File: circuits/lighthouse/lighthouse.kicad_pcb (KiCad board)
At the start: 2 copper layers, 4 parts, among them U1 ESP32 CP2102, U3 DCDC_StepUp_SX1308

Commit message: Circuits
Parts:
- added D1: LED, LED_SMD:LED_1206_3216Metric_Pad1.42x1.75mm_HandSolder, F.Cu at (117.8, 91.8)
- added D2: LED, LED_SMD:LED_1206_3216Metric_Pad1.42x1.75mm_HandSolder, F.Cu at (117.8, 94.8)
- added D3: LED, LED_SMD:LED_1206_3216Metric_Pad1.42x1.75mm_HandSolder, F.Cu at (117.8, 97.8)
- added D4: LED, LED_SMD:LED_1206_3216Metric_Pad1.42x1.75mm_HandSolder, F.Cu at (117.8, 100.8)
- added Q1: S9013, Package_TO_SOT_THT:TO-92_Inline, F.Cu at (125.3, 86.8)
- added R1: 10k, Resistor_SMD:R_1206_3216Metric_Pad1.30x1.75mm_HandSolder, F.Cu at (117.8, 103.8)
- added R2: 20k, Resistor_SMD:R_1206_3216Metric_Pad1.30x1.75mm_HandSolder, F.Cu at (123.8, 103.8)
- added R3: 1k, Resistor_SMD:R_1206_3216Metric_Pad1.30x1.75mm_HandSolder, F.Cu at (123.8, 91.8)
- added R4: 1k, Resistor_SMD:R_1206_3216Metric_Pad1.30x1.75mm_HandSolder, F.Cu at (123.8, 94.8)
- added R5: 1k, Resistor_SMD:R_1206_3216Metric_Pad1.30x1.75mm_HandSolder, F.Cu at (123.8, 97.8)
- added R6: 1k, Resistor_SMD:R_1206_3216Metric_Pad1.30x1.75mm_HandSolder, F.Cu at (123.8, 100.8)
- added R7: 240, LED_SMD:LED_1206_3216Metric_Pad1.42x1.75mm_HandSolder, F.Cu at (117.8, 88.8)
- added U2: DCDC_StepUp_SX1308, SX1308_DCDC_boost:DCDC_StepUp_SX1308, F.Cu at (91.0, 113.1)
- BT1: footprint Battery:BatteryHolder_MPD_BK-18650-PC2 -> Battery:BatteryHolder_MPD_BH-18650-PC
- U3: value DCDC_StepUp_SX1308 -> ~; footprint SX1308_DCDC_boost:DCDC_StepUp_SX1308 -> YR300:YR300
- moved U1 79.6 mm to (109.8, 94.8), turned to -90 degrees
- moved BT1 68.9 mm to (61.2, 140.3)
- moved CH1 68.6 mm to (72.8, 118.7)
- moved U3 67.2 mm to (119.3, 80.8), turned to 90 degrees
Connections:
- U1 pad 16: unconnected-(U1-GPIO9_/_SO2-Pad16) -> RX
- U1 pad 17: unconnected-(U1-GPIO10__/_S03-Pad17) -> TX
- U1 pad 19: Net-(U1-V5) -> 5V
- U1 pad 3: unconnected-(U1-GPIO36-Pad3) -> RFID_PW
- U1 pad 36: unconnected-(U1-GPIO22-Pad36) -> PWR_SENSE
- U1 pad 38: Net-(U1-GND-Pad38) -> GND
- U1 pad 4: unconnected-(U1-GPIO39-Pad4) -> MQTT_STS
- U1 pad 5: unconnected-(U1-GPIO34-Pad5) -> WIFI_STS
- U1 pad 6: unconnected-(U1-GPIO35-Pad6) -> SCAN_DETECTED
- U1 pad 7: unconnected-(U1-GPIO32-Pad7) -> ACTIVE_SCAN
- U3 pad 1: Net-(CH1-+OUT) -> 5V
- U3 pad 2: Net-(CH1--OUT) -> TX
- U3 pad 3: Net-(U1-GND-Pad38) -> RX
- U3 pad 4: Net-(U1-V5) -> Net-(Q1-C)
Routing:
- net 5V: track 0.00 -> 135.6 mm
- net Net-(U1-GND-Pad38): track 73.9 -> 0.00 mm
- net GND: track 0.00 -> 67.4 mm
- net Net-(Q1-C): track 0.00 -> 51.7 mm
- net ACTIVE_SCAN: track 0.00 -> 29.6 mm
- net SCAN_DETECTED: track 0.00 -> 25.8 mm
- net WIFI_STS: track 0.00 -> 22.1 mm
- net PWR_SENSE: track 0.00 -> 20.5 mm
- net Net-(BT1--): track 61.5 -> 80.3 mm
- net MQTT_STS: track 0.00 -> 18.3 mm
- net RFID_PW: track 0.00 -> 14.6 mm
- net Net-(U1-V5): track 12.2 -> 0.00 mm
- net Net-(Q1-B): track 0.00 -> 5.85 mm
- net RX: track 0.00 -> 5.21 mm
- net TX: track 0.00 -> 4.71 mm
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
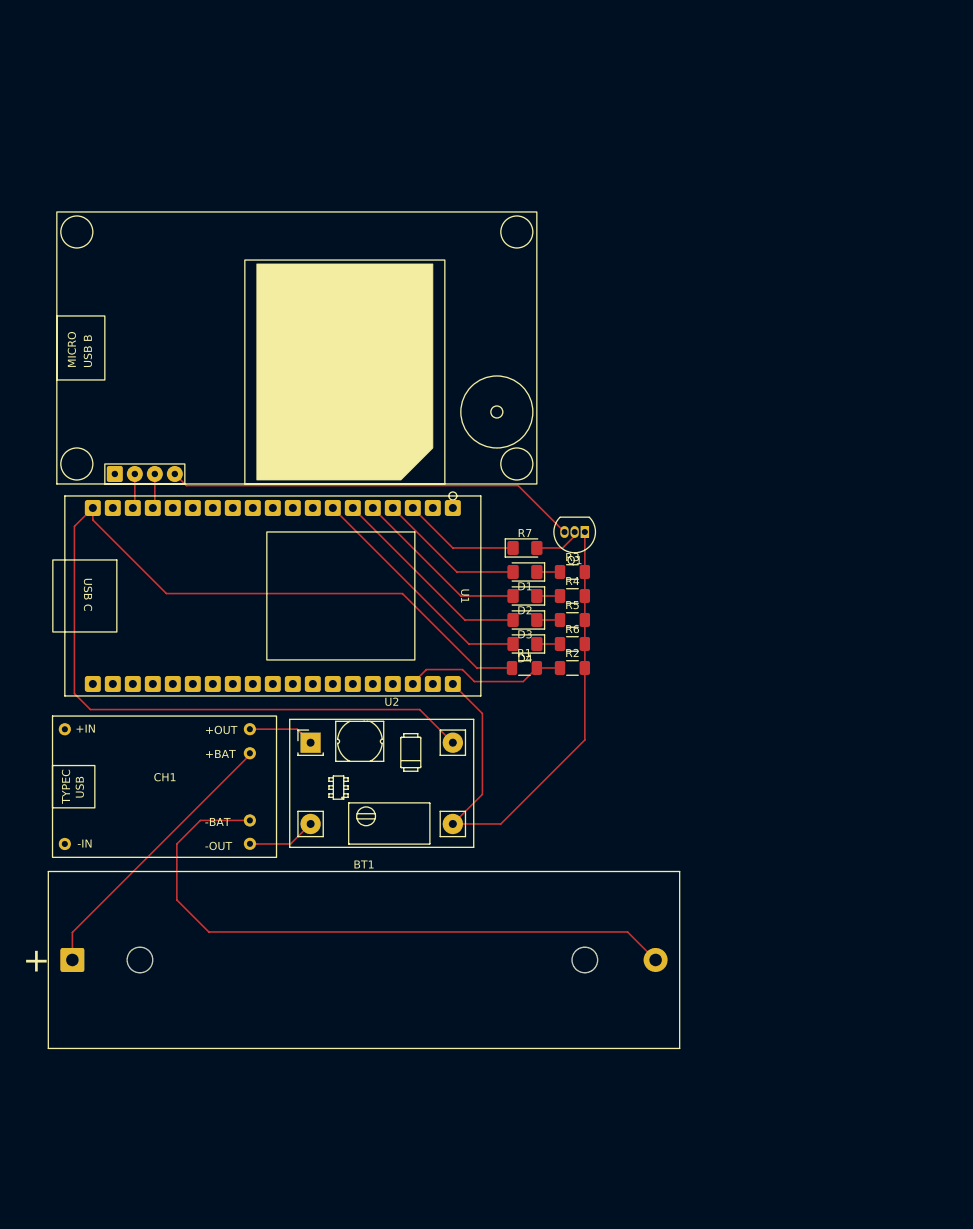
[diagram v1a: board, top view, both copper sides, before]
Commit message: Reverse engineered cell charger (component values missing)
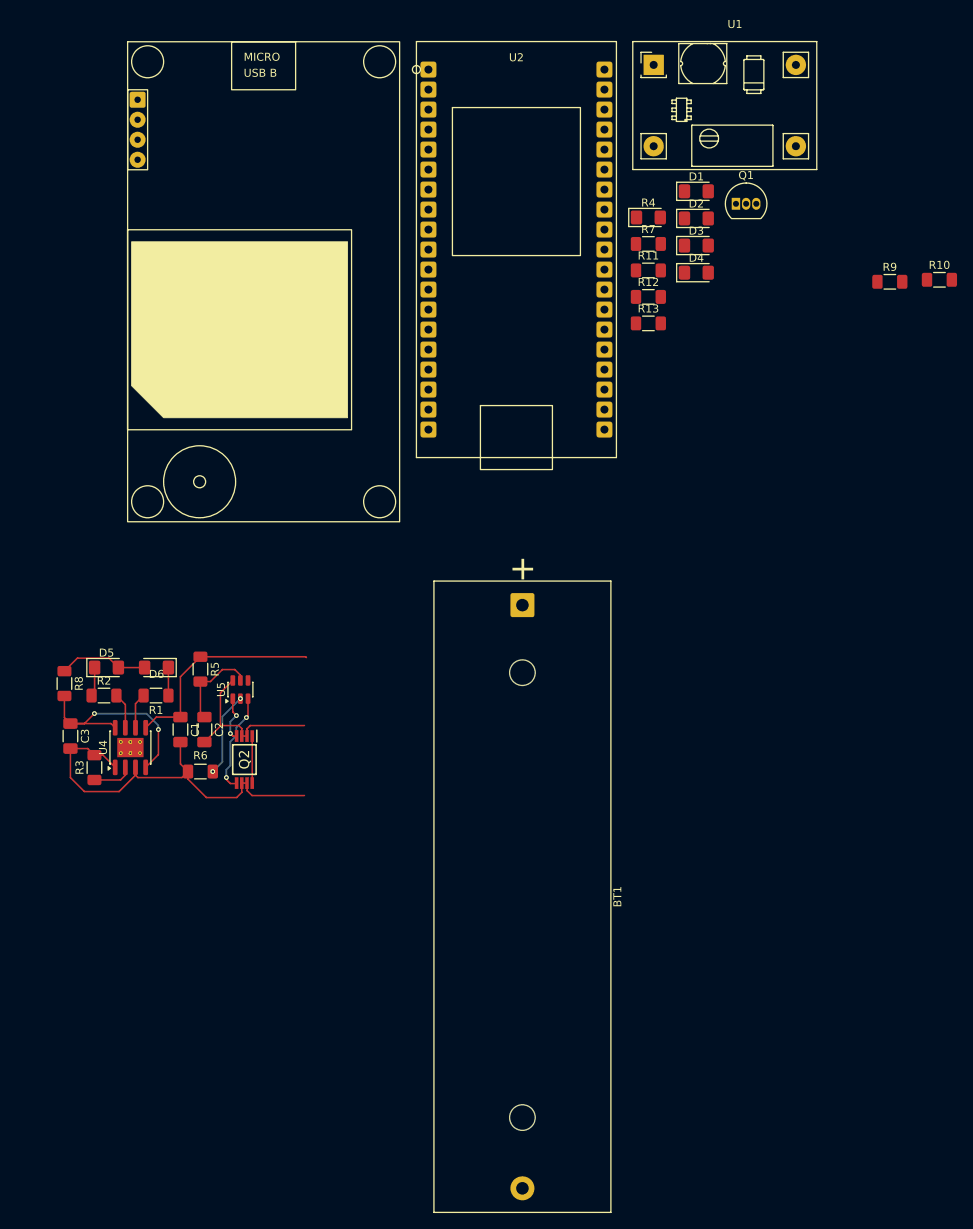
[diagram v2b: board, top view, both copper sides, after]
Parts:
- removed CH1: ~, TP4056_Charging_module:TP4056_Charging_Module_Type_C
- added C1: C, Capacitor_SMD:C_1206_3216Metric_Pad1.33x1.80mm_HandSolder, F.Cu at (74.8, 111.5)
- added C2: C, Capacitor_SMD:C_1206_3216Metric_Pad1.33x1.80mm_HandSolder, F.Cu at (77.8, 111.5)
- added C3: C, Capacitor_SMD:C_1206_3216Metric_Pad1.33x1.80mm_HandSolder, F.Cu at (61.0, 112.3)
- added D5: D, LED_SMD:LED_1206_3216Metric_Pad1.42x1.75mm_HandSolder, F.Cu at (65.5, 103.8)
- added D6: D, LED_SMD:LED_1206_3216Metric_Pad1.42x1.75mm_HandSolder, F.Cu at (71.8, 103.8)
- added Q2: FS8205A, FS8205A:SOP65P640X120-8N, F.Cu at (82.8, 115.2)
- added R10: 1k, Resistor_SMD:R_1206_3216Metric_Pad1.30x1.75mm_HandSolder, F.Cu at (169.6, 55.3)
- added R11: 1k, Resistor_SMD:R_1206_3216Metric_Pad1.30x1.75mm_HandSolder, F.Cu at (133.2, 54.1)
- added R12: 1k, Resistor_SMD:R_1206_3216Metric_Pad1.30x1.75mm_HandSolder, F.Cu at (133.2, 57.4)
- added R13: 1k, Resistor_SMD:R_1206_3216Metric_Pad1.30x1.75mm_HandSolder, F.Cu at (133.2, 60.7)
- added R8: R, Resistor_SMD:R_1206_3216Metric_Pad1.30x1.75mm_HandSolder, F.Cu at (60.2, 105.8)
- added R9: 20k, Resistor_SMD:R_1206_3216Metric_Pad1.30x1.75mm_HandSolder, F.Cu at (163.4, 55.5)
- added U4: TP4056-42-ESOP8, Package_SO:SOIC-8-1EP_3.9x4.9mm_P1.27mm_EP2.41x3.3mm_ThermalVias, F.Cu at (68.5, 113.8)
- added U5: DW01A, Package_TO_SOT_SMD:SOT-23-6, F.Cu at (82.2, 106.5)
- R1: value 10k -> 1k
- R2: value 20k -> 1k
- R3, R5, R6: value 1k -> R
- R4: value 1k -> 240; footprint Resistor_SMD:R_1206_3216Metric_Pad1.30x1.75mm_HandSolder -> LED_SMD:LED_1206_3216Metric_Pad1.42x1.75mm_HandSolder
- R7: value 240 -> 10k; footprint LED_SMD:LED_1206_3216Metric_Pad1.42x1.75mm_HandSolder -> Resistor_SMD:R_1206_3216Metric_Pad1.30x1.75mm_HandSolder
- U1: value ESP32 CP2102 -> DCDC_StepUp_SX1308; footprint ESP32:ESP32_38Pin -> SX1308_DCDC_boost:DCDC_StepUp_SX1308
- U2: value DCDC_StepUp_SX1308 -> ESP32 CP2102; footprint SX1308_DCDC_boost:DCDC_StepUp_SX1308 -> ESP32:ESP32_38Pin
- moved U2 88.9 mm to (116.8, 28.0)
- moved BT1 71.6 mm to (117.5, 95.9), turned to -90 degrees
- moved U1 70.6 mm to (133.9, 28.4), turned to 0 degrees
- moved R3 64.6 mm to (64.0, 116.2), turned to 90 degrees
- moved R2 58.7 mm to (65.2, 107.2)
- moved D1 52.2 mm to (139.2, 44.2), turned to 0 degrees
- moved D2 51.8 mm to (139.2, 47.6), turned to 0 degrees
- moved D3 51.5 mm to (139.2, 51.0), turned to 0 degrees
- moved U3 51.4 mm to (68.2, 85.5), turned to 0 degrees
- moved D4 51.1 mm to (139.2, 54.4), turned to 0 degrees
- moved R6 49.2 mm to (77.2, 116.8)
- moved R4 48.3 mm to (133.2, 47.5)
- moved R5 46.9 mm to (77.2, 104.0), turned to -90 degrees
- moved R1 46.2 mm to (71.7, 107.2), turned to 180 degrees
- moved Q1 45.2 mm to (144.2, 45.8), turned to 0 degrees
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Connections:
- BT1 pad 1: Net-(BT1-+) -> /Charger/+BAT
- BT1 pad 2: Net-(BT1--) -> /Charger/-BAT
- R1 pad 1: 5V -> Net-(D6-K)
- R1 pad 2: PWR_SENSE -> Net-(U4-~{STDBY})
- R2 pad 1: PWR_SENSE -> Net-(D5-K)
- R2 pad 2: GND -> Net-(U4-~{CHRG})
- R3 pad 1: Net-(D1-K) -> Net-(U4-PROG)
- R3 pad 2: GND -> /Charger/-IN
- R4 pad 1: Net-(D2-K) -> RFID_PW
- R4 pad 2: GND -> Net-(Q1-B)
- R5 pad 1: Net-(D3-K) -> /Charger/+BAT
- R5 pad 2: GND -> Net-(U5-VCC)
- R6 pad 1: Net-(D4-K) -> /Charger/-IN
- R6 pad 2: GND -> Net-(U5-CS)
- R7 pad 1: RFID_PW -> 5V
- R7 pad 2: Net-(Q1-B) -> PWR_SENSE
- U1 pad 1: unconnected-(U1-3V3-Pad1) -> /Charger/+BAT
- U1 pad 2: unconnected-(U1-EN-Pad2) -> /Charger/-IN
- U1 pad 3: RFID_PW -> GND
- U1 pad 4: MQTT_STS -> 5V
- U2 pad 1: Net-(CH1-+OUT) -> unconnected-(U2-3V3-Pad1)
- U2 pad 2: Net-(CH1--OUT) -> unconnected-(U2-EN-Pad2)
- U2 pad 3: GND -> RFID_PW
- U2 pad 4: 5V -> MQTT_STS
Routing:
- net 5V: track 135.6 -> 0.00 mm
- net Net-(BT1--): track 80.3 -> 0.00 mm
- net GND: track 67.4 -> 0.00 mm
- net Net-(Q1-C): track 51.7 -> 0.00 mm
- net /Charger/-IN: track 0.00 -> 51.0 mm
- net Net-(BT1-+): track 35.0 -> 0.00 mm
- net ACTIVE_SCAN: track 29.6 -> 0.00 mm
- net /Charger/+IN: track 0.00 -> 28.3 mm, vias 0 -> 2
- net /Charger/+BAT: track 0.00 -> 26.8 mm
- net SCAN_DETECTED: track 25.8 -> 0.00 mm
- net WIFI_STS: track 22.1 -> 0.00 mm
- net /Charger/-BAT: track 0.00 -> 21.8 mm
- net PWR_SENSE: track 20.5 -> 0.00 mm
- net MQTT_STS: track 18.3 -> 0.00 mm
- net RFID_PW: track 14.6 -> 0.00 mm
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
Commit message: More circuits
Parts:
- removed U3: ~, YR300:YR300
- added AE1: Antenna_Shield, Connector_Coaxial:SMA_Samtec_SMA-J-P-H-ST-EM1_EdgeMount, F.Cu at (95.9, 63.4)
- added BOOT1: SW_Push, Button_Switch_SMD:SW_Push_SPST_NO_Alps_SKRK, F.Cu at (-42.9, 104.0)
- added BZ1: Buzzer, Buzzer_Beeper:Buzzer_12x9.5RM7.6, F.Cu at (176.4, 60.7)
- added C10: C, Capacitor_SMD:C_1206_3216Metric_Pad1.33x1.80mm_HandSolder, F.Cu at (-33.7, 33.0)
- added C11: C, Capacitor_SMD:C_1206_3216Metric_Pad1.33x1.80mm_HandSolder, F.Cu at (-94.4, 94.8)
- added C12: C, Capacitor_SMD:C_1206_3216Metric_Pad1.33x1.80mm_HandSolder, F.Cu at (-94.4, 98.2)
- added C13: C, Capacitor_SMD:C_1206_3216Metric_Pad1.33x1.80mm_HandSolder, F.Cu at (-94.4, 101.5)
- added C4: C, Capacitor_SMD:C_1206_3216Metric_Pad1.33x1.80mm_HandSolder, F.Cu at (83.1, 127.2)
- added C5: C, Capacitor_SMD:C_1206_3216Metric_Pad1.33x1.80mm_HandSolder, F.Cu at (98.6, 122.8)
- added C6: C, Capacitor_SMD:C_1206_3216Metric_Pad1.33x1.80mm_HandSolder, F.Cu at (137.1, 122.5)
- added C7: C, Capacitor_SMD:C_1206_3216Metric_Pad1.33x1.80mm_HandSolder, F.Cu at (137.1, 120.0)
- added C8: C, Capacitor_SMD:C_1206_3216Metric_Pad1.33x1.80mm_HandSolder, F.Cu at (138.6, 92.7)
- added C9: C, Capacitor_SMD:C_1206_3216Metric_Pad1.33x1.80mm_HandSolder, F.Cu at (138.6, 96.0)
- added D10: D, LED_SMD:LED_1206_3216Metric_Pad1.42x1.75mm_HandSolder, F.Cu at (168.6, 64.3)
- added D11: LED, LED_SMD:LED_1206_3216Metric_Pad1.42x1.75mm_HandSolder, F.Cu at (133.1, 121.2)
- added D12: D_Schottky, Diode_SMD:D_2114_3652Metric_Pad1.85x3.75mm_HandSolder, F.Cu at (-63.1, 94.8)
- added D13: LED, LED_SMD:LED_1206_3216Metric_Pad1.42x1.75mm_HandSolder, F.Cu at (-75.2, 112.1)
- added D14: LED, LED_SMD:LED_1206_3216Metric_Pad1.42x1.75mm_HandSolder, F.Cu at (-99.9, 70.0)
- added D7: D_Schottky, Diode_SMD:D_2114_3652Metric_Pad1.85x3.75mm_HandSolder, F.Cu at (94.4, 117.8)
- added D8: LED, LED_SMD:LED_1206_3216Metric_Pad1.42x1.75mm_HandSolder, F.Cu at (144.6, 86.0)
- added D9: LED, LED_SMD:LED_1206_3216Metric_Pad1.42x1.75mm_HandSolder, F.Cu at (144.6, 89.4)
- added EN1: SW_Push, Button_Switch_SMD:SW_Push_SPST_NO_Alps_SKRK, F.Cu at (-42.9, 108.5)
- added IC1: SX1308, SX1308:SOT95P280X145-6N, F.Cu at (91.6, 122.8)
- added L1: L, Inductor_THT:L_Radial_L8.0mm_W8.0mm_P5.00mm_Neosid_SD8, F.Cu at (84.6, 117.2)
- added Q3: 2N7002K, Package_TO_SOT_SMD:SOT-23, F.Cu at (166.5, 67.5)
- added Q4: SS8050, Package_TO_SOT_SMD:SOT-23, F.Cu at (-16.9, 11.0)
- added Q5: SS8050, Package_TO_SOT_SMD:SOT-23, F.Cu at (-16.9, 15.4)
- added R14: R, Resistor_SMD:R_1206_3216Metric_Pad1.30x1.75mm_HandSolder, F.Cu at (85.6, 127.2)
- added R15: R, Resistor_SMD:R_1206_3216Metric_Pad1.30x1.75mm_HandSolder, F.Cu at (109.1, 97.0)
- added R16: R, Resistor_SMD:R_1206_3216Metric_Pad1.30x1.75mm_HandSolder, F.Cu at (144.5, 100.7)
- added R17: R, Resistor_SMD:R_1206_3216Metric_Pad1.30x1.75mm_HandSolder, F.Cu at (159.7, 67.5)
- added R18: R, Resistor_SMD:R_1206_3216Metric_Pad1.30x1.75mm_HandSolder, F.Cu at (162.2, 67.5)
- added R19: R, Resistor_SMD:R_1206_3216Metric_Pad1.30x1.75mm_HandSolder, F.Cu at (140.9, 121.2)
- added R20: 10k, Resistor_SMD:R_1206_3216Metric_Pad1.30x1.75mm_HandSolder, F.Cu at (-44.4, 21.8)
- added R21: 10k, Resistor_SMD:R_1206_3216Metric_Pad1.30x1.75mm_HandSolder, F.Cu at (-112.2, 59.0)
- added R22: 10k, Resistor_SMD:R_1206_3216Metric_Pad1.30x1.75mm_HandSolder, F.Cu at (-112.2, 62.2)
- added R23: 1k, Resistor_SMD:R_1206_3216Metric_Pad1.30x1.75mm_HandSolder, F.Cu at (-112.2, 65.5)
- added R24: 1k, Resistor_SMD:R_1206_3216Metric_Pad1.30x1.75mm_HandSolder, F.Cu at (-75.7, 115.2)
- added R25: 10k, Resistor_SMD:R_1206_3216Metric_Pad1.30x1.75mm_HandSolder, F.Cu at (-75.7, 118.6)
- added R26: 10k, Resistor_SMD:R_1206_3216Metric_Pad1.30x1.75mm_HandSolder, F.Cu at (-40.3, 30.5)
- added R27: 10k, Resistor_SMD:R_1206_3216Metric_Pad1.30x1.75mm_HandSolder, F.Cu at (-27.6, 17.2)
- added R28: 1k, Resistor_SMD:R_1206_3216Metric_Pad1.30x1.75mm_HandSolder, F.Cu at (-29.4, 27.8)
- added R29: 1k, Resistor_SMD:R_1206_3216Metric_Pad1.30x1.75mm_HandSolder, F.Cu at (-21.2, 23.0)
- added R30: 10k, Resistor_SMD:R_1206_3216Metric_Pad1.30x1.75mm_HandSolder, F.Cu at (-37.9, 16.5)
- added R31: 1k, Resistor_SMD:R_1206_3216Metric_Pad1.30x1.75mm_HandSolder, F.Cu at (95.6, 122.8)
- added RV1: 8k4, Varistor:RV_Disc_D7mm_W4.9mm_P5mm, F.Cu at (95.1, 129.2)
- added U10: CP2102-GMR, CP2102-GMR:QFN28_5X5_SIL, F.Cu at (-35.9, 24.7)
- added U6: AMS1117-3.3, Package_TO_SOT_SMD:SOT-223-3_TabPin2, F.Cu at (162.9, 61.0)
- added U7: ESP32-WROOM-32, RF_Module:ESP32-WROOM-32, F.Cu at (61.3, 79.2)
- U1: value DCDC_StepUp_SX1308 -> R300; footprint SX1308_DCDC_boost:DCDC_StepUp_SX1308 -> YR300:R300
- U2: value ESP32 CP2102 -> AMS1117-3.3; footprint ESP32:ESP32_38Pin -> Package_TO_SOT_SMD:SOT-223-3_TabPin2
- moved R10 263.6 mm to (-93.9, 59.6)
- moved R9 257.3 mm to (-93.9, 56.3)
- moved D1 239.3 mm to (-99.9, 53.0)
- moved D2 239.3 mm to (-99.9, 56.4)
- moved D3 239.3 mm to (-99.9, 59.8)
- moved D4 239.3 mm to (-99.9, 63.2)
- moved R11 227.3 mm to (-93.9, 62.9)
- moved R12 227.3 mm to (-93.9, 66.2)
- moved R13 227.3 mm to (-93.9, 69.6)
- moved R7 227.2 mm to (-93.9, 53.0)
- moved U2 95.3 mm to (106.2, 122.7), turned to 180 degrees
- moved BT1 77.7 mm to (56.7, 144.2), turned to 0 degrees
- moved Q1 77.3 mm to (80.6, 89.8)
- moved R4 62.9 mm to (82.6, 84.8)
- moved U1 43.1 mm to (118.0, 68.5), turned to 180 degrees
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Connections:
- C1 pad 2: /Charger/-IN -> GND
- C3 pad 2: /Charger/-IN -> GND
- Q1 pad 3: Net-(Q1-C) -> /R300/GND
- Q2 pad 6: /Charger/-IN -> GND
- Q2 pad 7: /Charger/-IN -> GND
- R3 pad 2: /Charger/-IN -> GND
- R6 pad 1: /Charger/-IN -> GND
- R7 pad 2: PWR_SENSE -> Net-(U7-IO22)
- R9 pad 1: PWR_SENSE -> Net-(U7-IO22)
- U1 pad 1: /Charger/+BAT -> Net-(AE1-A)
- U1 pad 2: /Charger/-IN -> Net-(AE1-Shield)
- U1 pad 3: GND -> Net-(AE1-Shield)
- U1 pad 4: 5V -> Net-(AE1-Shield)
- U2 pad 1: unconnected-(U2-3V3-Pad1) -> GND
- U2 pad 2: unconnected-(U2-EN-Pad2) -> 3.3V
- U2 pad 3: RFID_PW -> 5V
- U4 pad 1: /Charger/-IN -> GND
- U4 pad 3: /Charger/-IN -> GND
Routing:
- net GND: track 0.00 -> 65.8 mm
- net /Charger/-BAT: track 21.8 -> 81.1 mm, vias 0 -> 1
- net /Charger/-IN: track 51.0 -> 0.00 mm
- net /Charger/+BAT: track 26.8 -> 73.3 mm, vias 0 -> 1
- net 5V: track 0.00 -> 27.7 mm
- net Net-(D7-A): track 0.00 -> 16.0 mm
- net Net-(BZ1--): track 0.00 -> 14.7 mm
- net Net-(AE1-Shield): track 0.00 -> 12.7 mm
- net Net-(D11-K): track 0.00 -> 8.52 mm
- net Net-(IC1-FB): track 0.00 -> 8.33 mm
- net Net-(Q3-G): track 0.00 -> 6.13 mm
- net Net-(C6-Pad1): track 0.00 -> 6.11 mm
- net /R300/GND: track 0.00 -> 6.09 mm
- net Net-(R14-Pad1): track 0.00 -> 5.14 mm
- net Net-(AE1-A): track 0.00 -> 4.97 mm

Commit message: The circuit now has all the values in place
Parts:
- added C14: 10u, Capacitor_SMD:C_1206_3216Metric_Pad1.33x1.80mm_HandSolder, F.Cu at (100.7, 105.4)
- added J1: USB_C_Receptacle_PowerOnly_6P, Connector_USB:USB_C_Receptacle_GCT_USB4125-xx-x_6P_TopMnt_Horizontal, F.Cu at (42.0, 111.4)
- added J2: USB_B_Micro, Connector_USB:USB_Micro-B_Amphenol_10103594-0001LF_Horizontal, F.Cu at (44.2, 96.5)
- added R32: 5k1, Resistor_SMD:R_1206_3216Metric_Pad1.30x1.75mm_HandSolder, F.Cu at (48.0, 114.1)
- added R33: 5k1, Resistor_SMD:R_1206_3216Metric_Pad1.30x1.75mm_HandSolder, F.Cu at (48.0, 108.6)
- C1: value C -> 22u
- C10: value C -> 56n
- C11: value C -> 1u
- C12, C6, C8: value C -> 10u
- C13: value C -> 150n
- C2, C3: value C -> 100n
- C7: value C -> 15n
- C9: value C -> 22n
- L1: value L -> 4R7
- R14: value R -> 200
- R15, R18: value R -> 10k
- R16, R17: value R -> 1k
- R19: value R -> 5k1
- R3: value R -> 820
- R4: footprint LED_SMD:LED_1206_3216Metric_Pad1.42x1.75mm_HandSolder -> Resistor_SMD:R_1206_3216Metric_Pad1.30x1.75mm_HandSolder
- R5: value R -> 100 (470)
- R6: value R -> 1k0
- R8: value R -> 2
- moved C12 203.1 mm to (108.2, 110.9)
- moved C13 202.7 mm to (108.2, 107.1)
- moved R21 195.4 mm to (79.5, 97.2), turned to 180 degrees
- moved R23 193.5 mm to (79.5, 92.2), turned to 180 degrees
- moved R22 190.0 mm to (75.2, 93.8), turned to 90 degrees
- moved R7 185.3 mm to (89.0, 82.5), turned to -90 degrees
- moved R9 181.8 mm to (86.0, 82.5), turned to 90 degrees
- moved D14 181.1 mm to (79.5, 94.8)
- moved D1 177.5 mm to (73.8, 89.8), turned to 180 degrees
- moved R10 176.0 mm to (79.5, 89.8)
- moved D3 175.2 mm to (73.8, 83.0), turned to 180 degrees
- moved D4 175.1 mm to (73.8, 86.2), turned to 180 degrees
- moved D2 174.5 mm to (73.7, 74.5), turned to 180 degrees
- moved R12 174.2 mm to (79.5, 83.0)
- moved R13 174.2 mm to (79.5, 86.2)
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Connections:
- net /Charger/+IN renamed Net-(U4-CE)
- BZ1 pad 1: 5V -> +5V
- C12 pad 1: 3.3V -> +3.3V
- C13 pad 1: 3.3V -> +3.3V
- C5 pad 1: 5V -> +5V
- C6 pad 1: Net-(C6-Pad1) -> /R300/GND
- C6 pad 2: 5V -> +5V
- C7 pad 1: Net-(C6-Pad1) -> /R300/GND
- C7 pad 2: 5V -> +5V
- C8 pad 1: 5V -> +5V
- C8 pad 2: Net-(BZ1--) -> /R300/GND
- C9 pad 1: 5V -> +5V
- C9 pad 2: Net-(BZ1--) -> /R300/GND
- D10 pad 1: 5V -> +5V
- D11 pad 2: 5V -> +5V
- D12 pad 1: 3.3V -> +3.3V
- D14 pad 2: 3.3V -> +3.3V
- D7 pad 1: 5V -> +5V
- R15 pad 1: 5V -> +5V
- R17 pad 2: /R300/GND -> Net-(D8-A)
- R19 pad 2: Net-(C6-Pad1) -> /R300/GND
- R20 pad 1: 3.3V -> +3.3V
- R21 pad 1: 3.3V -> +3.3V
- R25 pad 1: 3.3V -> +3.3V
- R30 pad 1: 3.3V -> +3.3V
- R31 pad 1: 5V -> +5V
- R7 pad 1: 5V -> /R300/GND
- U1 pad 9: 5V -> +5V
- U10 pad 29: unconnected-(U10-EPAD-Pad29) -> GND
- U10 pad 4: unconnected-(U10-D+-Pad4) -> Net-(J2-D+)
- U10 pad 5: unconnected-(U10-D--Pad5) -> Net-(J2-D-)
- U10 pad 7: 3.3V -> +5V
- U10 pad 8: unconnected-(U10-VBUS-Pad8) -> +3.3V
- U2 pad 2: 3.3V -> +3.3V
- U2 pad 3: 5V -> +5V
- U4 pad 9: unconnected-(U4-EPAD-Pad9) -> GND
- U6 pad 1: Net-(BZ1--) -> /R300/GND
- U6 pad 2: 5V -> +5V
- U6 pad 3: 5V -> +5V
- U7 pad 2: 3.3V -> +3.3V
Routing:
- net +3.3V: track 0.00 -> 127.7 mm, vias 0 -> 4
- net +5V: track 0.00 -> 119.8 mm, vias 0 -> 2
- net GND: track 65.8 -> 167.3 mm, vias 0 -> 10
- net ESP25: track 0.00 -> 53.1 mm, vias 0 -> 2
- net /R300/GND: track 6.09 -> 58.0 mm, vias 0 -> 5
- net TX: track 0.00 -> 40.5 mm, vias 0 -> 4
- net RX: track 0.00 -> 36.5 mm, vias 0 -> 2
- net EN: track 0.00 -> 28.2 mm
- net 5V: track 27.7 -> 0.00 mm
- net MP24: track 0.00 -> 27.5 mm, vias 0 -> 2
- net MP28: track 0.00 -> 27.5 mm, vias 0 -> 2
- net Net-(U7-IO22): track 0.00 -> 27.1 mm
- net ESP35: track 0.00 -> 27.1 mm, vias 0 -> 2
- net ESP34: track 0.00 -> 25.4 mm, vias 0 -> 2
- net MQTT_STS: track 0.00 -> 21.2 mm
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- added copper zone on B.Cu, net GND
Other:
- board outline added: 84 x 112 mm

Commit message: Board v1
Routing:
- net ESP24: track 8.39 -> 13.3 mm
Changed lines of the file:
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@@
 	)
 	(segment
-		(start 67.1925 94.8725)
-		(end 63.58 91.26)
+		(start 71.7015 92.961)
+		(end 72.4 92.2625)
 		(width 0.2)
 		(layer "F.Cu")
@@
 		(width 0.2)
 		(layer "F.Cu")
+		(net 24)
+	)
+	(segment
+		(start 65.811 92.961)
+		(end 71.7015 92.961)
+		(width 0.2)
+		(layer "F.Cu")
+		(net 24)
+	)
+	(segment
+		(start 63.58 90.73)
+		(end 65.811 92.961)
+		(width 0.2)
+		(layer "F.Cu")
